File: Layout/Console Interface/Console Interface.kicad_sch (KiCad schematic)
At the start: 0 parts

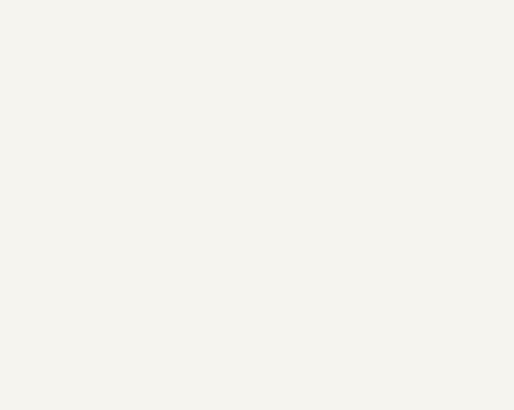
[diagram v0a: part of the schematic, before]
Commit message: Add console interface schematic
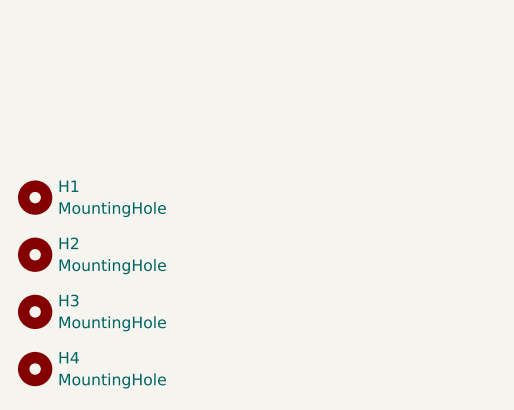
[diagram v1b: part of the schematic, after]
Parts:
- added H1, H2, H3, H4: MountingHole, MountingHole:MountingHole_2.2mm_M2, symbol Mechanical:MountingHole
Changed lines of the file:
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@@
 (kicad_sch (version 20230121) (generator eeschema)
   (paper "A4")
+  (symbol (lib_id "Mechanical:MountingHole") (at 41.91 158.75 0) (unit 1)
+    (in_bom yes) (on_board yes) (dnp no) (fields_autoplaced)
+    (property "Reference" "H2" (at 44.45 157.5379 0)
+      (effects (font (size 1.27 1.27)) (justify left))
+    )
+    (property "Value" "MountingHole" (at 44.45 159.9621 0)
+      (effects (font (size 1.27 1.27)) (justify left))
+    )
+    (property "Footprint" "MountingHole:MountingHole_2.2mm_M2" (at 41.91 158.75 0)
+      (effects (font (size 1.27 1.27)) hide)
+    )
+    (property "Datasheet" "~" (at 41.91 158.75 0)
+      (effects (font (size 1.27 1.27)) hide)
+    )
+    (instances
+      (project "Console Interface"
+        (path "/de034696-2c40-409b-8cc3-cb3d87a6597e"
+          (reference "H2") (unit 1)
+        )
+      )
+    )
+  )
+  (symbol (lib_id "Mechanical:MountingHole") (at 41.91 152.4 0) (unit 1)
+    (in_bom yes) (on_board yes) (dnp no) (fields_autoplaced)
+    (property "Reference" "H1" (at 44.45 151.1879 0)
+      (effects (font (size 1.27 1.27)) (justify left))
+    )
+    (property "Value" "MountingHole" (at 44.45 153.6121 0)
+      (effects (font (size 1.27 1.27)) (justify left))
+    )
+    (property "Footprint" "MountingHole:MountingHole_2.2mm_M2" (at 41.91 152.4 0)
+      (effects (font (size 1.27 1.27)) hide)
+    )
+    (property "Datasheet" "~" (at 41.91 152.4 0)
+      (effects (font (size 1.27 1.27)) hide)
+    )
+    (instances
+      (project "Console Interface"
+        (path "/de034696-2c40-409b-8cc3-cb3d87a6597e"
+          (reference "H1") (unit 1)
+        )
+      )
+    )
+  )
+  (symbol (lib_id "Mechanical:MountingHole") (at 41.91 165.1 0) (unit 1)
+    (in_bom yes) (on_board yes) (dnp no) (fields_autoplaced)
+    (property "Reference" "H3" (at 44.45 163.8879 0)
+      (effects (font (size 1.27 1.27)) (justify left))
+    )
+    (property "Value" "MountingHole" (at 44.45 166.3121 0)
+      (effects (font (size 1.27 1.27)) (justify left))
+    )
+    (property "Footprint" "MountingHole:MountingHole_2.2mm_M2" (at 41.91 165.1 0)
+      (effects (font (size 1.27 1.27)) hide)
+    )
+    (property "Datasheet" "~" (at 41.91 165.1 0)
+      (effects (font (size 1.27 1.27)) hide)
+    )
+    (instances
+      (project "Console Interface"
+        (path "/de034696-2c40-409b-8cc3-cb3d87a6597e"
+          (reference "H3") (unit 1)
+        )
+      )
+    )
+  )
+  (symbol (lib_id "Mechanical:MountingHole") (at 41.91 171.45 0) (unit 1)
+    (in_bom yes) (on_board yes) (dnp no) (fields_autoplaced)
+    (property "Reference" "H4" (at 44.45 170.2379 0)
+      (effects (font (size 1.27 1.27)) (justify left))
+    )
+    (property "Value" "MountingHole" (at 44.45 172.6621 0)
+      (effects (font (size 1.27 1.27)) (justify left))
+    )
+    (property "Footprint" "MountingHole:MountingHole_2.2mm_M2" (at 41.91 171.45 0)
+      (effects (font (size 1.27 1.27)) hide)
+    )
+    (property "Datasheet" "~" (at 41.91 171.45 0)
+      (effects (font (size 1.27 1.27)) hide)
+    )
+    (instances
+      (project "Console Interface"
+        (path "/de034696-2c40-409b-8cc3-cb3d87a6597e"
+          (reference "H4") (unit 1)
+        )
+      )
+    )
+  )
   (sheet (at 139.446 89.027) (size 63.627 37.973) (fields_autoplaced)
     (stroke (width 0.1524) (type solid))
